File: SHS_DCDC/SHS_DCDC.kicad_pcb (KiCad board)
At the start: 4 copper layers, 100 x 100 mm, 107 parts, among them J1 Barrel_Jack, J2 USB_A, J3 Conn_ARM_JTAG_SWD_10, Q1 BSS84, Q10 PMV100XPEAR, Q11 PMV100XPEAR, Q12 PMV100XPEAR, Q13 PMV100XPEAR, Q14 PMV100XPEAR, Q15 BSS84, Q16 PMV100XPEAR, Q17 PMV100XPEAR, Q2 PMV100XPEAR, Q3 2N7002, Q4 2N7002, Q5 PMV100XPEAR, Q6 2N7002, Q7 PMV100XPEAR, Q8 Q_PMOS_DGS, Q9 PMV100XPEAR, U1 RT8299-WDFN10L, U2 INA181, U3 LMV324AIDR, U4 LMV358IDR, U5 MP3414A, U6 ESP32-S2-MINI-1, U7 MCP101

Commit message: ProgressMisc
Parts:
- added C2: TBD, Capacitor_SMD:C_0402_1005Metric, F.Cu at (25.4, 81.6)
- added C37: TBD, Capacitor_SMD:C_0402_1005Metric, F.Cu at (25.4, 79.0)
- added Y1: 2-SMD no lead, Crystal:Crystal_SMD_3215-2Pin_3.2x1.5mm, F.Cu at (22.8, 80.3)
- moved C4 10.9 mm to (35.0, 54.2), turned to 0 degrees
- moved C5 8.08 mm to (35.0, 59.7), turned to 0 degrees
- moved C3 4.10 mm to (47.2, 62.1), turned to 90 degrees
- moved R15 3.32 mm to (49.6, 62.9), turned to 180 degrees
- moved C29 1.08 mm to (8.45, 88.3)
- moved R14 1.00 mm to (49.6, 61.3), turned to 0 degrees
- moved Q13 0.07 mm to (30.1, 73.1)
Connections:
- U6 pad 19: unconnected-(U6-Pad19) -> Net-(U6-Pad19)
- U6 pad 20: unconnected-(U6-Pad20) -> Net-(U6-Pad20)
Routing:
- net USB_D-: track 0.00 -> 99.9 mm, vias 0 -> 1
- net USB_D+: track 0.00 -> 97.2 mm, vias 0 -> 1
- net V_MCU: track 52.0 -> 14.6 mm, vias 0 -> 9
- net DCDC_OUT: track 53.2 -> 67.5 mm
- net MCU_RST: track 9.55 -> 22.5 mm
- net Net-(U6-Pad19): track 0.00 -> 5.59 mm
- net Net-(U6-Pad20): track 0.00 -> 5.57 mm
- net Net-(Q4-Pad3): track 0.00 -> 5.49 mm
- net LOAD: track 78.5 -> 82.5 mm
- net Net-(C11-Pad1): track 0.07 -> 3.94 mm
- net Net-(Q2-Pad1): track 2.00 -> 5.49 mm
- net OP_V2-: track 0.00 -> 3.39 mm
- net MCU_PWM_MPPT: track 40.1 -> 37.4 mm
- net OP_VS+: track 0.00 -> 1.38 mm
- net LOAD_BULB1: track 21.1 -> 20.6 mm
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- added copper zone on F.Cu, net V_MCU
- added copper zone on In1.Cu, net V_MCU

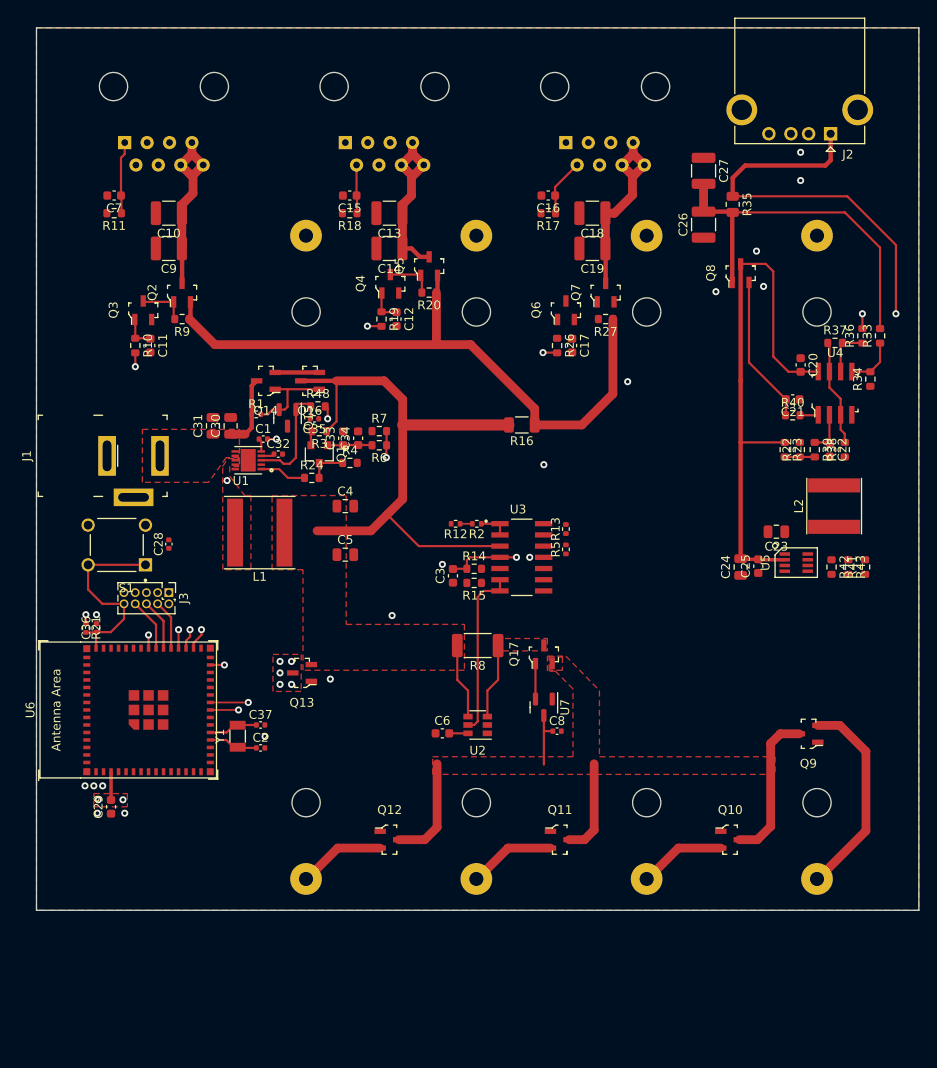
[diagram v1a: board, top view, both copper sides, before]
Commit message: Bif fix
Big fix on DCDCOUT and LOAD signal
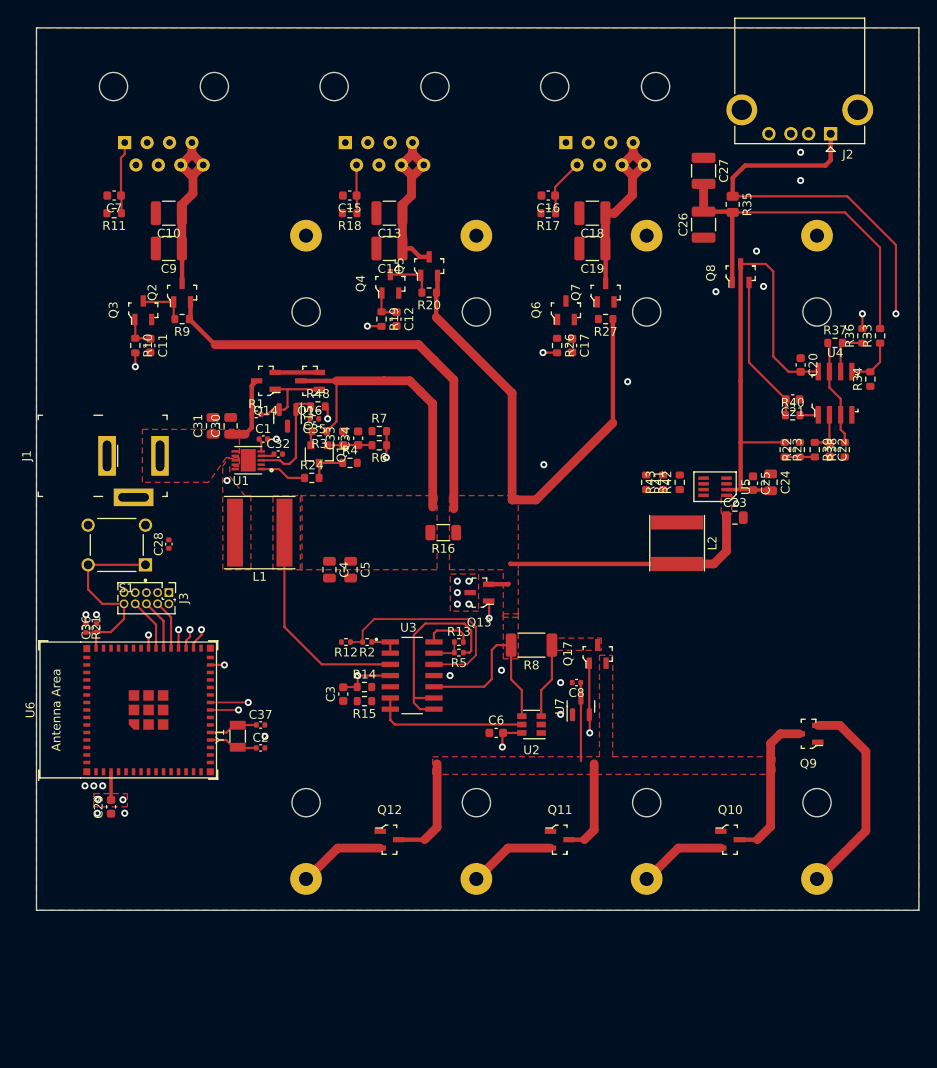
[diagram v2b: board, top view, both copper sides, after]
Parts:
- moved R41 26.6 mm to (69.1, 51.5), turned to -90 degrees
- moved R43 23.1 mm to (71.0, 51.5), turned to 90 degrees
- moved Q13 22.1 mm to (50.2, 64.0)
- moved R42 19.7 mm to (72.9, 51.5), turned to 90 degrees
- moved L2 18.3 mm to (72.6, 58.4), turned to -90 degrees
- moved R14 18.3 mm to (37.2, 74.7)
- moved U3 18.3 mm to (42.6, 73.4)
- moved C3 18.3 mm to (34.8, 75.5)
- moved R15 18.3 mm to (37.2, 76.3)
- moved R12 18.3 mm to (35.1, 69.6)
- moved R2 18.3 mm to (37.5, 69.6)
- moved R13 17.6 mm to (47.9, 69.6), turned to 0 degrees
- moved R5 16.9 mm to (47.9, 70.8), turned to 180 degrees
- moved R16 15.1 mm to (46.1, 57.2)
- moved U5 12.6 mm to (76.9, 52.0), turned to 90 degrees
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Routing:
- net LOAD: track 82.5 -> 157.7 mm
- net ODP_RESET: track 4.01 -> 32.3 mm, vias 0 -> 2
- net OP_VS+: track 1.38 -> 24.8 mm
- net OP_V1-: track 0.00 -> 23.2 mm
- net DCDC_OUT: track 67.5 -> 58.5 mm
- net 5V: track 63.0 -> 55.2 mm
- net OP_VS: track 0.00 -> 5.49 mm
- net OP_VS-: track 0.00 -> 3.54 mm
- net VBAT: track 46.8 -> 49.1 mm
- net VREF_BIDIRECTIONAL: track 19.4 -> 17.6 mm
- net V_MCU: track 14.6 -> 14.5 mm, vias 9 -> 10
- added copper zone on F.Cu, net LOAD

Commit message: OCP
Adding overcharge protection
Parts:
- added C38: 100nF, Capacitor_SMD:C_0402_1005Metric, F.Cu at (68.5, 65.5)
- added C39: 10uF, Capacitor_SMD:C_0805_2012Metric, F.Cu at (56.0, 64.7)
- added C40: 1uF, Capacitor_SMD:C_0603_1608Metric, F.Cu at (63.1, 65.5)
- added R25: 100k, Resistor_SMD:R_0402_1005Metric, F.Cu at (74.6, 65.5)
- added U8: MIC5501-3.0YM5, Package_TO_SOT_SMD:SOT-23-5, F.Cu at (60.1, 64.7)
- added U9: BD49LxxG, Package_TO_SOT_SMD:SOT-23, F.Cu at (71.4, 66.4)
- Q13: footprint digikey-footprints:SOT-23-3 -> digikey-kicad-library-master:SOT-23-3
- R11, R17, R18: value 10k -> 100k
- moved Q13 22.3 mm to (71.4, 71.0), turned to -90 degrees
- moved C26 16.2 mm to (91.5, 19.1), turned to 180 degrees
- moved C27 15.9 mm to (91.5, 15.7), turned to 180 degrees
- moved Q8 13.2 mm to (79.8, 41.0)
- moved Q17 13.0 mm to (76.4, 73.0)
- moved C8 13.0 mm to (72.9, 79.8), turned to 0 degrees
- moved U7 10.7 mm to (72.4, 77.1), turned to -90 degrees
- moved R36 9.24 mm to (94.5, 44.1), turned to -90 degrees
- moved R35 6.60 mm to (78.9, 26.6)
- moved C28 0.61 mm to (14.4, 58.6)
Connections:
- Q13 pad 1: ODP_RESET -> OCP_BAT
- Q13 pad 2: LOAD -> VBAT_SW
- Q13 pad 3: V_MCU -> Net-(Q13-Pad3)
- Q17 pad 3: Net-(Q17-Pad3) -> Net-(Q13-Pad3)
- R8 pad 1: Net-(Q17-Pad3) -> VBAT_SW
- U2 pad 3: Net-(Q17-Pad3) -> VBAT_SW
- U6 pad 26: unconnected-(U6-Pad26) -> MCU_BL2_ONOFFSIG
- U6 pad 5: unconnected-(U6-Pad5) -> MCU_OCP_BAT
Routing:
- net V_MCU: track 14.5 -> 109.2 mm, vias 10 -> 11
- net MCU_OCP_BAT: track 0.00 -> 80.6 mm, vias 0 -> 2
- net MCU_BL2_ONOFFSIG: track 6.51 -> 81.2 mm, vias 0 -> 2
- net VBAT_SW: track 0.00 -> 14.5 mm
- net 5V: track 55.2 -> 43.3 mm
- net Net-(C21-Pad2): track 16.8 -> 6.02 mm
- net Net-(L2-Pad1): track 0.00 -> 9.46 mm
- net Net-(C26-Pad2): track 51.1 -> 60.0 mm, vias 2 -> 0
- net Net-(Q17-Pad3): track 8.55 -> 0.00 mm
- net Net-(R41-Pad2): track 0.00 -> 7.97 mm
- net Net-(Q8-Pad1): track 42.0 -> 34.8 mm
- net ODP_RESET: track 32.3 -> 25.4 mm
- net OCP_BAT: track 0.00 -> 6.19 mm
- net Net-(Q6-Pad3): track 0.00 -> 5.59 mm
- net VBAT: track 49.1 -> 43.7 mm
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- added copper zone on F.Cu, net Net-(Q13-Pad3)
- added copper zone on F.Cu, net VBAT_SW
- added copper zone on In2.Cu, net V_MCU
- removed copper zone on F.Cu, net Net-(Q17-Pad3)
- removed copper zone on In1.Cu, net V_MCU

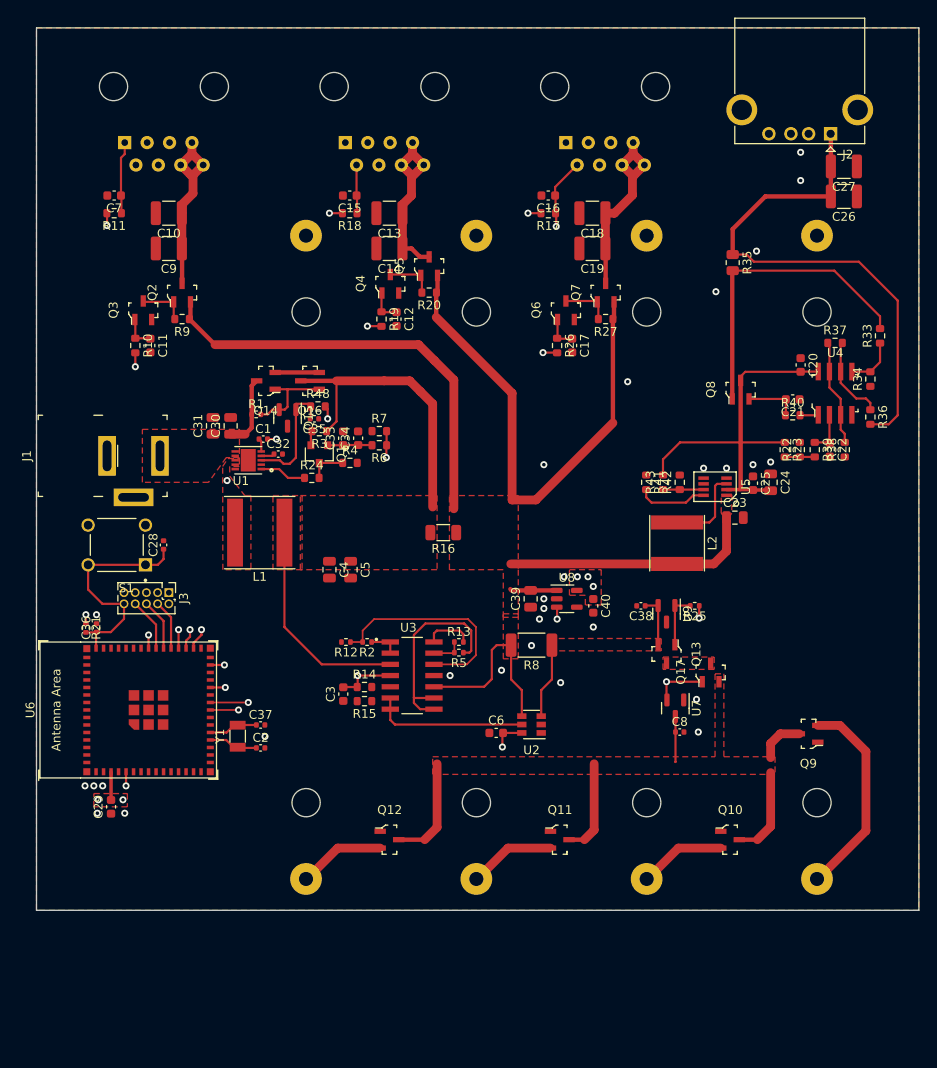
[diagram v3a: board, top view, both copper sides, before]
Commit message: 6 layers PCB
Decision to move to a 6 layers PCB to ease the PCB routing
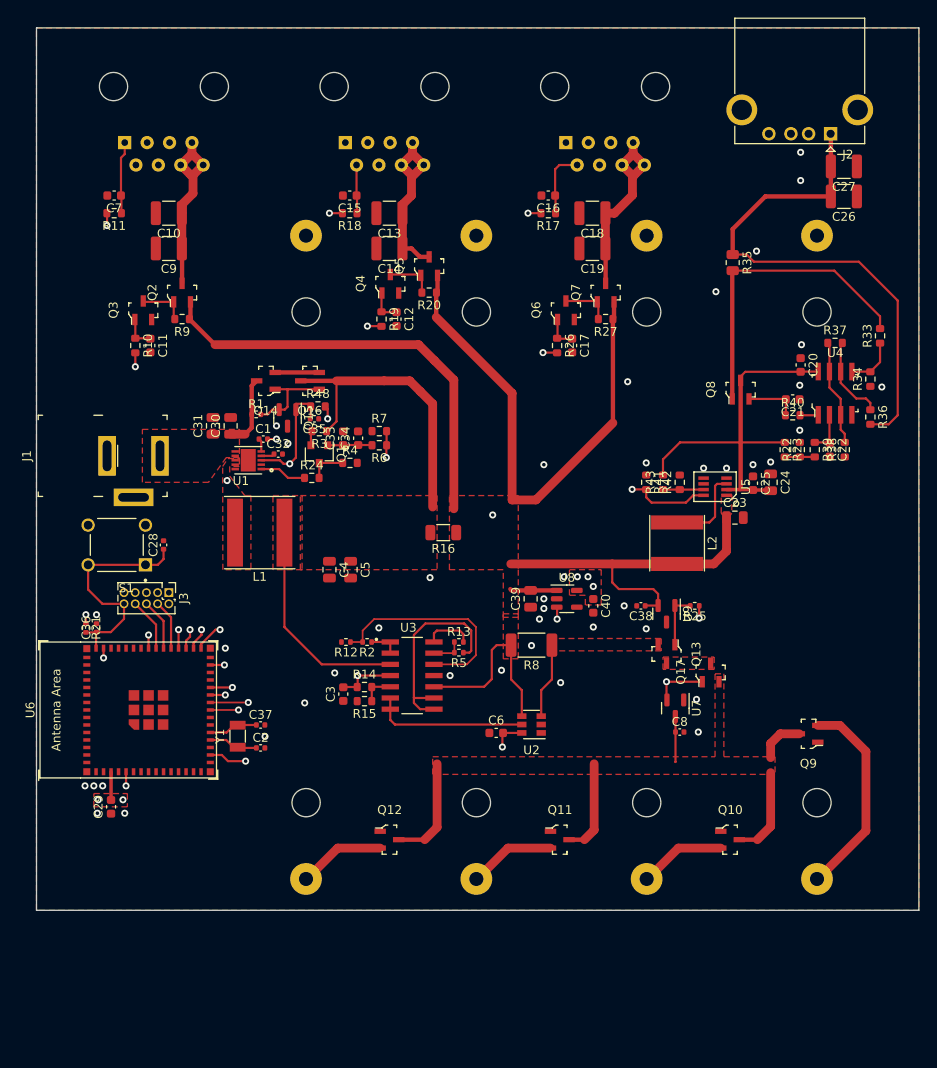
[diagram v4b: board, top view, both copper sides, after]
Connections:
- C38 pad 1: VBAT_SW -> LOAD
- R41 pad 1: MCU_5V_EN -> GND
- R41 pad 2: Net-(R41-Pad2) -> MCU_5V_EN
- U5 pad 8: Net-(R41-Pad2) -> MCU_5V_EN
- U6 pad 17: unconnected-(U6-Pad17) -> MCU_5V_EN
- U6 pad 25: unconnected-(U6-Pad25) -> MCU_BL2_ONOFFSIG
- U6 pad 26: MCU_BL2_ONOFFSIG -> MCU_BL1_ONOFFSIG
- U6 pad 31: unconnected-(U6-Pad31) -> MCU_MPPT_ENABLE
- U6 pad 44: unconnected-(U6-Pad44) -> MCU_TL_ONOFFSIG
- U9 pad 2: VBAT_SW -> LOAD
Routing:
- net MCU_5V_EN: track 0.00 -> 70.4 mm, vias 0 -> 2
- net MCU_BL1_ONOFFSIG: track 5.18 -> 74.5 mm, vias 0 -> 1
- net MCU_TL_ONOFFSIG: track 7.80 -> 71.7 mm, vias 0 -> 1
- net MCU_MPPT_ENABLE: track 13.7 -> 42.2 mm, vias 0 -> 2
- net LOAD: track 162.7 -> 173.3 mm
- net Net-(R41-Pad2): track 7.97 -> 0.00 mm
- net MCU_BL2_ONOFFSIG: track 81.2 -> 89.1 mm, vias 2 -> 1
- net V_MCU: track 109.2 -> 115.2 mm
- net VBAT_SW: track 14.5 -> 8.55 mm
- net Net-(R14-Pad2): track 0.00 -> 3.71 mm
- net MCU_OCP_BAT: track 80.6 -> 82.3 mm
- net GND: vias 29 -> 44
- added copper zone on In4.Cu, net GND
- added copper zone on In3.Cu, net V_MCU
- removed copper zone on In2.Cu, net V_MCU
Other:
- copper layers 4 -> 6

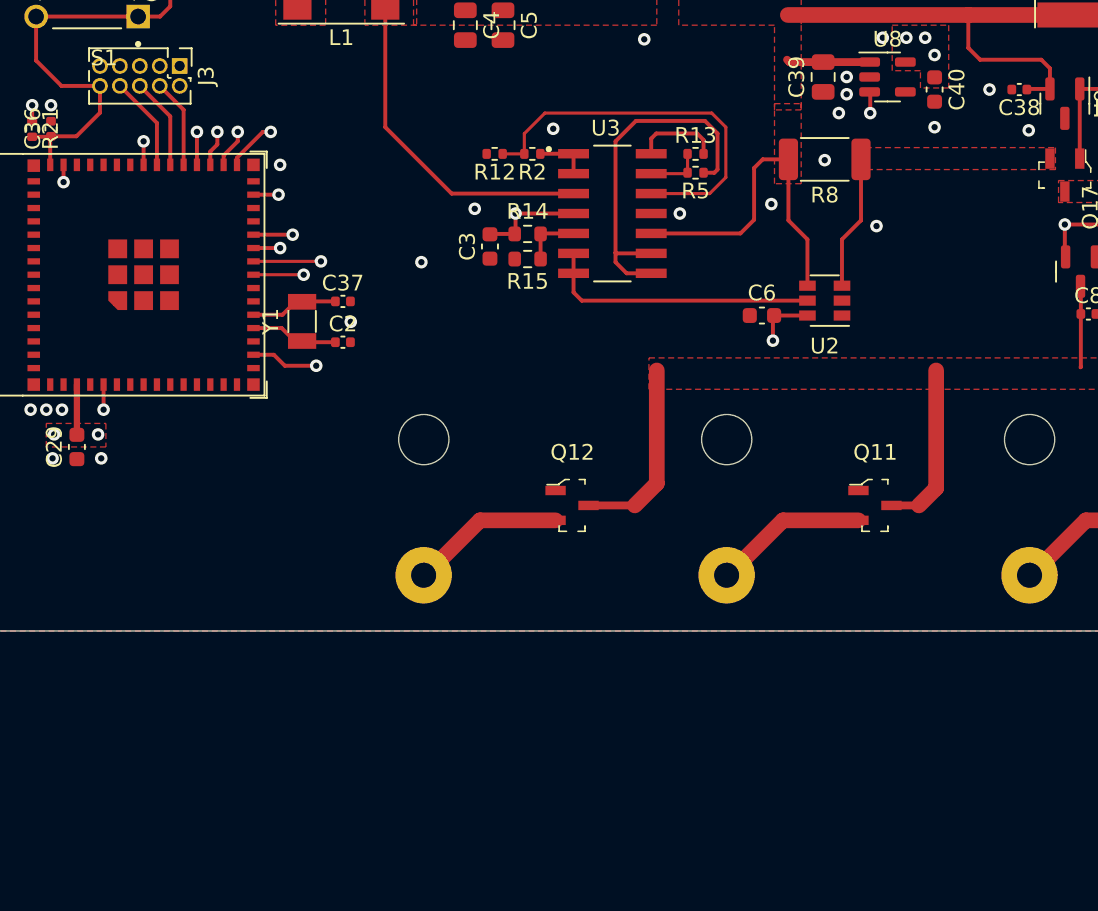
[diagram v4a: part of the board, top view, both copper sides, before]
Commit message: PV & BAT V sense
Adding 2 same blocks allowing the measure by ADC of the PV and Battery voltage on demand through power gating technique
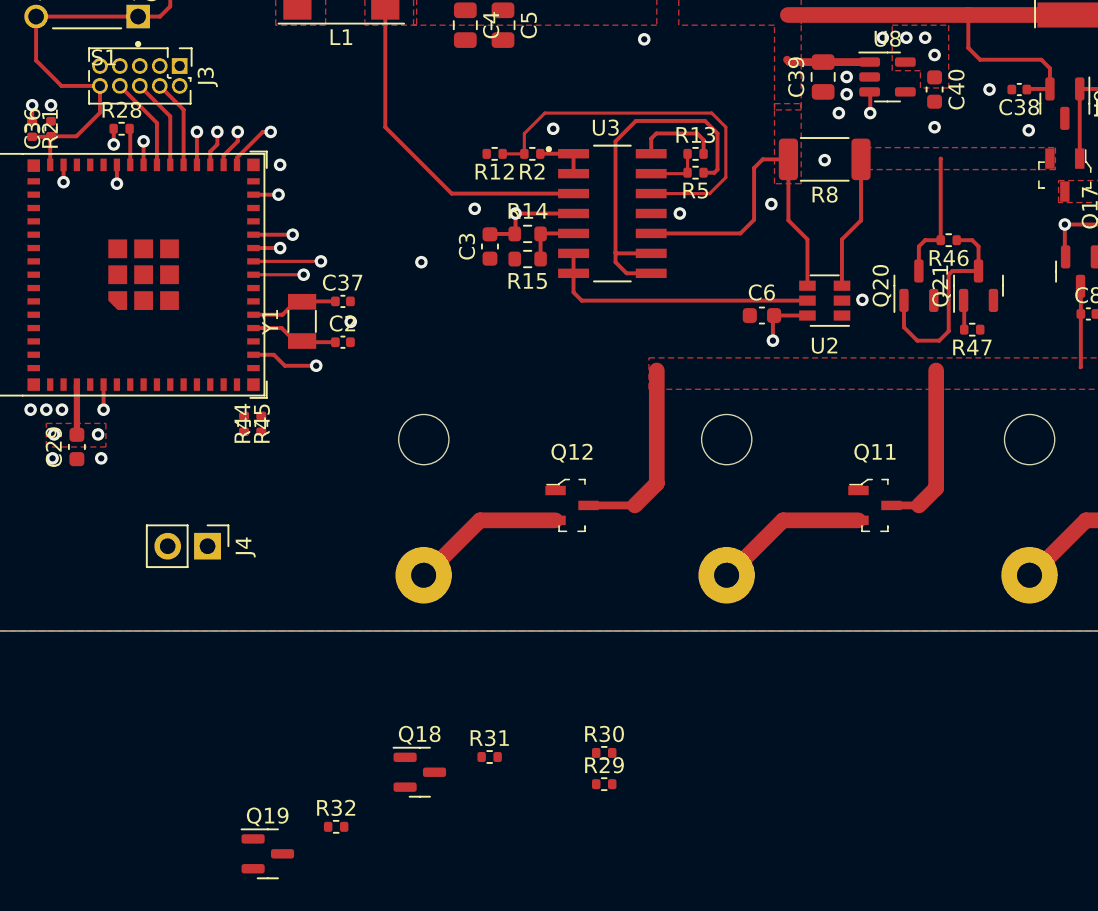
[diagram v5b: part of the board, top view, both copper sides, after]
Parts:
- added J4: Conn_01x02_Male, Connector_PinHeader_2.54mm:PinHeader_1x02_P2.54mm_Vertical, F.Cu at (16.8, 94.6)
- added Q18: BSS84, Package_TO_SOT_SMD:SOT-23, F.Cu at (30.3, 109.0)
- added Q19: 2N7002, Package_TO_SOT_SMD:SOT-23, F.Cu at (20.6, 114.2)
- added Q20: BSS84, Package_TO_SOT_SMD:SOT-23, F.Cu at (62.1, 78.0)
- added Q21: 2N7002, Package_TO_SOT_SMD:SOT-23, F.Cu at (65.9, 78.0)
- added R28: 499, Resistor_SMD:R_0402_1005Metric, F.Cu at (11.3, 68.0)
- added R29: 10k, Resistor_SMD:R_0402_1005Metric, F.Cu at (42.0, 109.8)
- added R30: 10k, Resistor_SMD:R_0402_1005Metric, F.Cu at (42.0, 107.8)
- added R31: 100k, Resistor_SMD:R_0402_1005Metric, F.Cu at (34.8, 108.0)
- added R32: 100k, Resistor_SMD:R_0402_1005Metric, F.Cu at (25.0, 112.5)
- added R44: 10k, Resistor_SMD:R_0402_1005Metric, F.Cu at (20.2, 86.8)
- added R45: 10k, Resistor_SMD:R_0402_1005Metric, F.Cu at (19.1, 86.8)
- added R46: 100k, Resistor_SMD:R_0402_1005Metric, F.Cu at (64.0, 75.1)
- added R47: 100k, Resistor_SMD:R_0402_1005Metric, F.Cu at (65.5, 80.8)
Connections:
- net Net-(C30-Pad1) renamed PV
- U6 pad 39: unconnected-(U6-Pad39) -> Net-(R28-Pad2)
- U6 pad 40: unconnected-(U6-Pad40) -> MCU_RX
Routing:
- net MCU_TX: track 0.00 -> 28.5 mm, vias 0 -> 1
- net MCU_RX: track 0.00 -> 26.7 mm, vias 0 -> 1
- net Net-(Q20-Pad1): track 0.00 -> 13.9 mm
- net VBAT_SW: track 8.55 -> 16.9 mm
- net Net-(R28-Pad2): track 0.00 -> 2.32 mm
- net MCU_ADC_BAT_CTRL: track 0.00 -> 1.88 mm
